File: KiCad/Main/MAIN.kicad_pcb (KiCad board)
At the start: 4 copper layers, 99.6 x 99.8 mm, 92 parts, among them J1 Conn_01x32_Socket, J2 Conn_02x05_Odd_Even, J3 Conn_01x32_Socket, Q1 BC558, Q2 BC548, Q3 BC558, Q4 BC548, Q5 BC558, Q6 BC548, U1 40106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

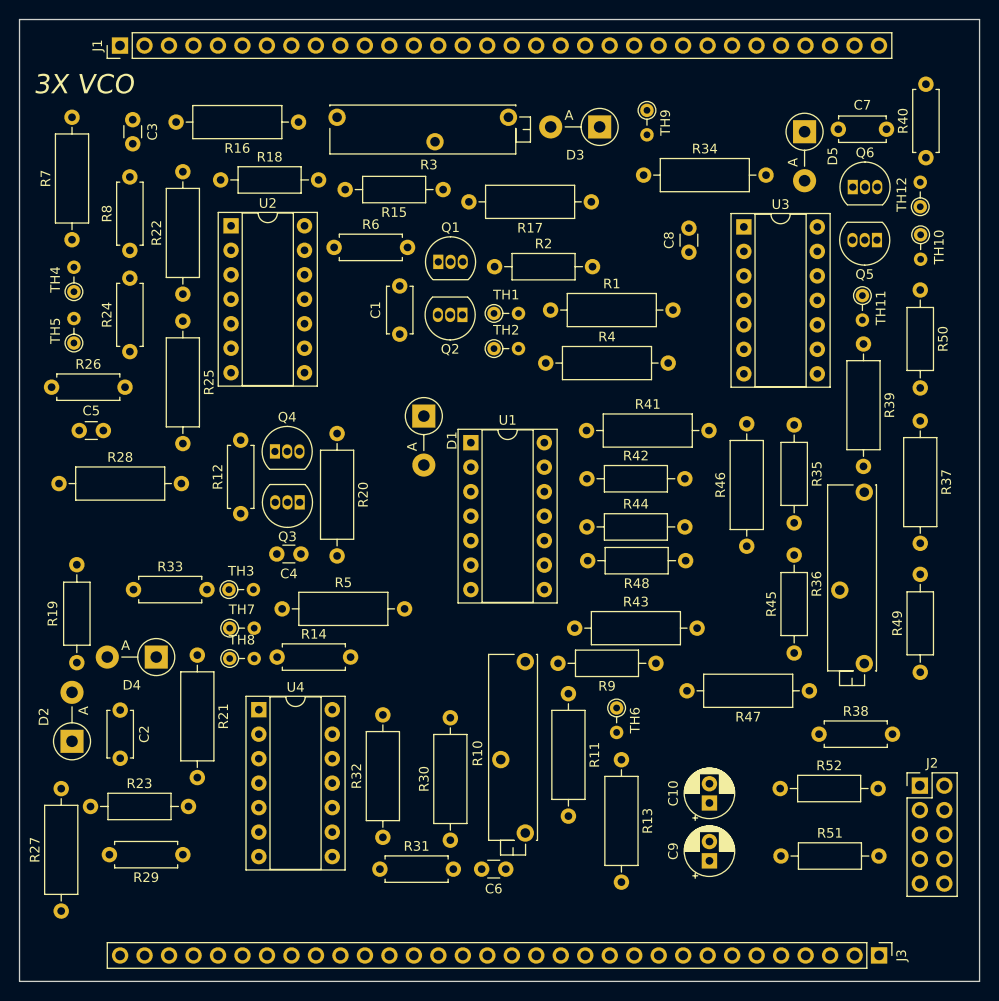
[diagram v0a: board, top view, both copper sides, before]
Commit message: fix: Missing PCB traces in main board project & gerbers
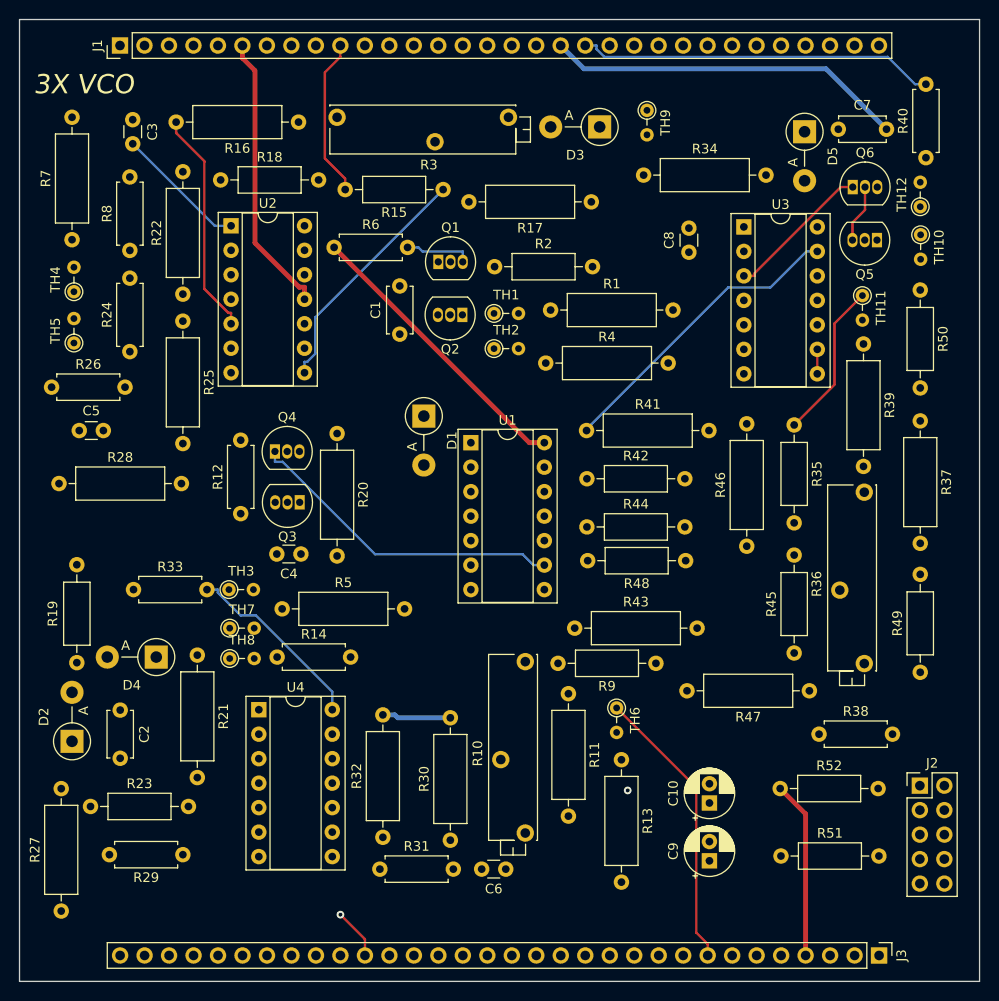
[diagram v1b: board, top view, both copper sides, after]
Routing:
- net VCO1CoarsePot1: track 0.00 -> 419.7 mm
- net VCO1CoarsePot3: track 0.00 -> 289.5 mm
- net VCO2IDKPot1: track 0.00 -> 228.4 mm
- net SW2p2: track 0.00 -> 137.8 mm
- net VCO2PwmPot2: track 0.00 -> 114.9 mm
- net VCO3FMPot2: track 0.00 -> 110.4 mm
- net SW1p2: track 0.00 -> 108.1 mm
- net fmIn2: track 0.00 -> 108.0 mm
- net VCO3FMPot1: track 0.00 -> 98.8 mm
- net Net-(D2-K): track 0.00 -> 97.6 mm
- net VCO1FMPot1: track 0.00 -> 82.4 mm
- net VCO3PwmPot1: track 0.00 -> 80.9 mm
- net fmIn1: track 0.00 -> 78.6 mm
- net VCO3FinePot2: track 0.00 -> 77.4 mm
- net VCO2CoarsePot2: track 0.00 -> 72.2 mm
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
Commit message: refactor: Rework Main board PCB
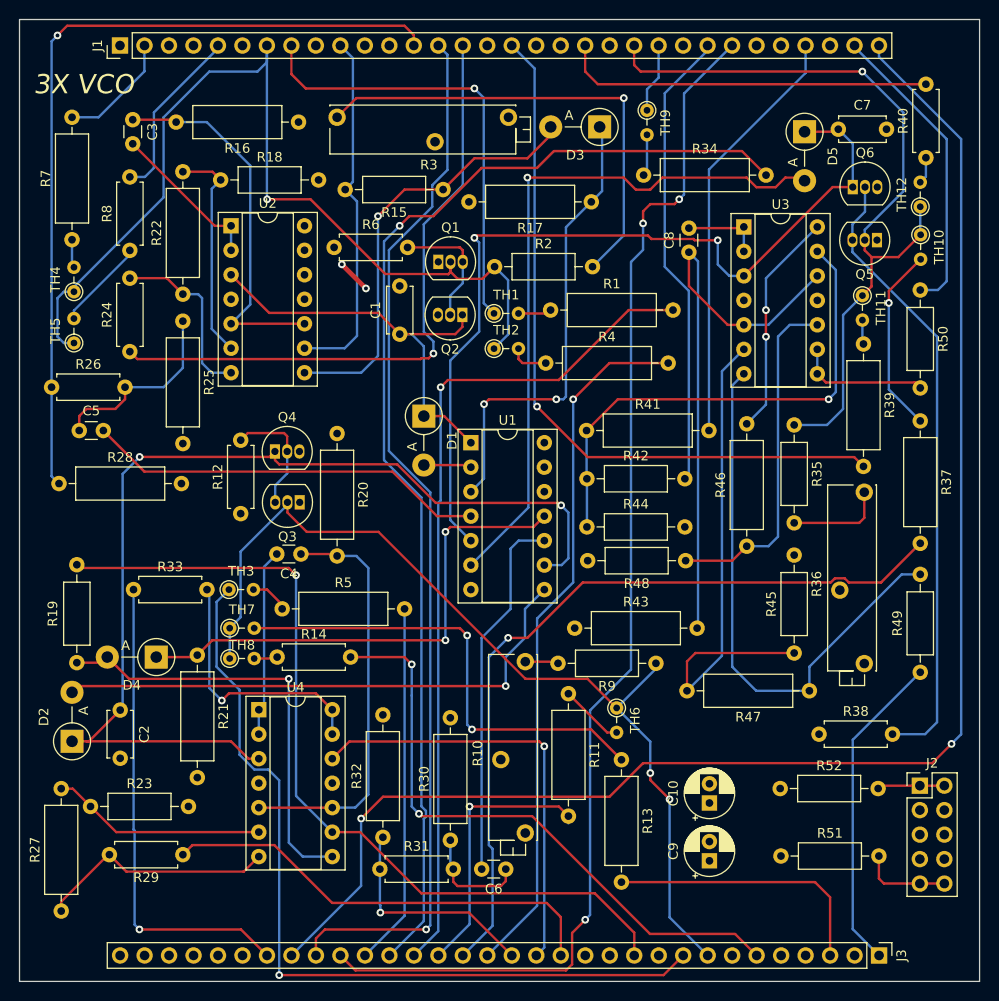
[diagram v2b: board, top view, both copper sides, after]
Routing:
- net VCO1CoarsePot1: track 419.7 -> 0.00 mm
- net VCO3FMPot2: track 110.4 -> 86.8 mm, vias 0 -> 1
- net Net-(D5-K): track 68.1 -> 90.4 mm, vias 0 -> 2
- net SW2p2: track 137.8 -> 158.0 mm, vias 0 -> 2
- net SW1p1: track 65.9 -> 85.9 mm, vias 0 -> 1
- net VCO1FMPot1: track 82.4 -> 100.2 mm, vias 0 -> 1
- net Net-(D5-A): track 56.8 -> 73.5 mm, vias 0 -> 1
- net Net-(R2-Pad2): track 32.9 -> 49.4 mm, vias 0 -> 1
- net cvIn2: track 66.5 -> 82.4 mm
- net VCO2FMPot1: track 64.9 -> 80.7 mm, vias 0 -> 1
- net SW1p3: track 51.6 -> 66.1 mm, vias 0 -> 1
- net fmIn2: track 108.0 -> 122.0 mm, vias 0 -> 1
- net VCO3FinePot2: track 77.4 -> 63.6 mm, vias 0 -> 2
- net VCO2PwmPot2: track 114.9 -> 128.6 mm, vias 0 -> 3
- net Net-(U3D--): track 41.7 -> 52.9 mm, vias 0 -> 1
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- added copper zone on In1.Cu, net VCO1CoarsePot1

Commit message: Update BOM
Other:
- board text added: "3xOsc"
- board text removed: "3X VCO"
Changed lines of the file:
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@@
 		(layer "Edge.Cuts")
 	)
-	(gr_text "3X VCO\n"
+	(gr_text "3xOsc\n"
 		(at 228.5 76 0)
 		(layer "F.SilkS")
